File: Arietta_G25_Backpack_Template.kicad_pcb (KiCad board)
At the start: 2 copper layers, 26.7 x 53.3 mm, 1 part, among them P1 HEADER_F_2.54MM_2R40P_ST_AU_P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

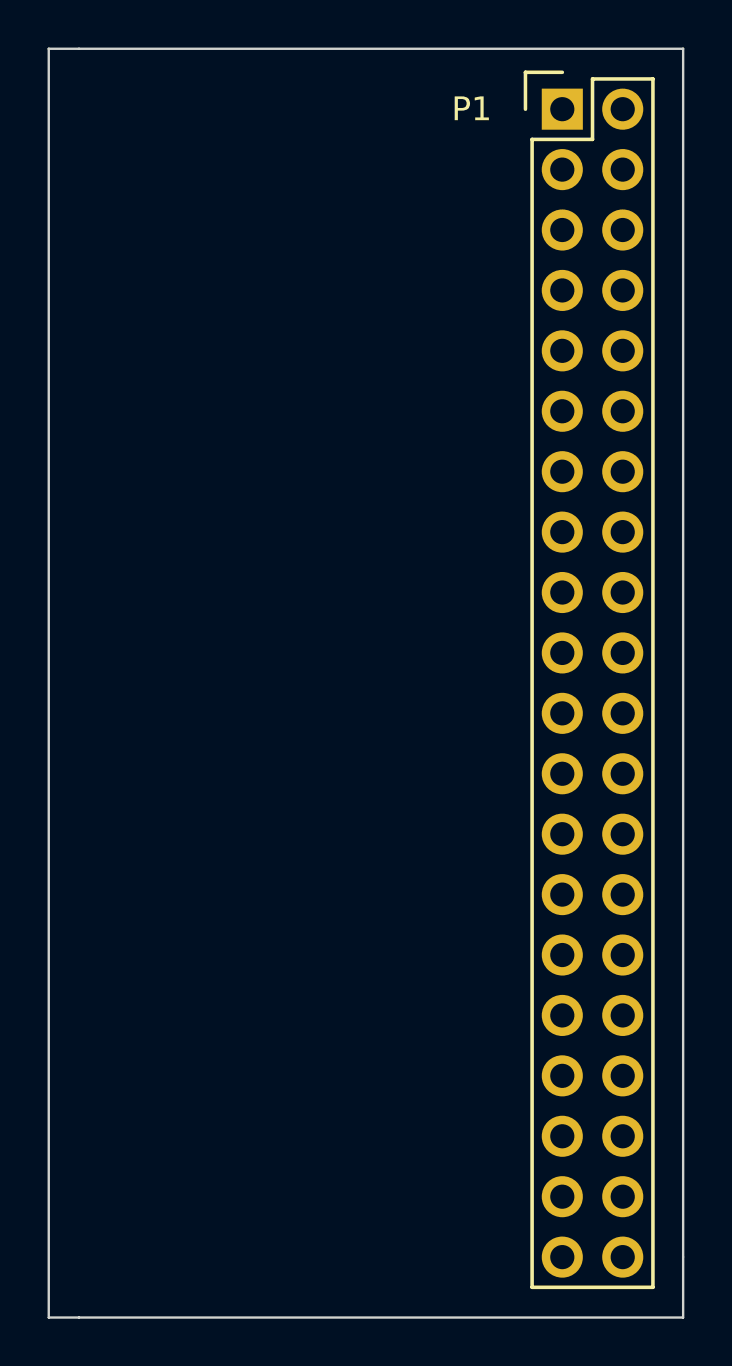
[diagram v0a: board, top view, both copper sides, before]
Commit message: Changed connector on PCB to use one in local library.
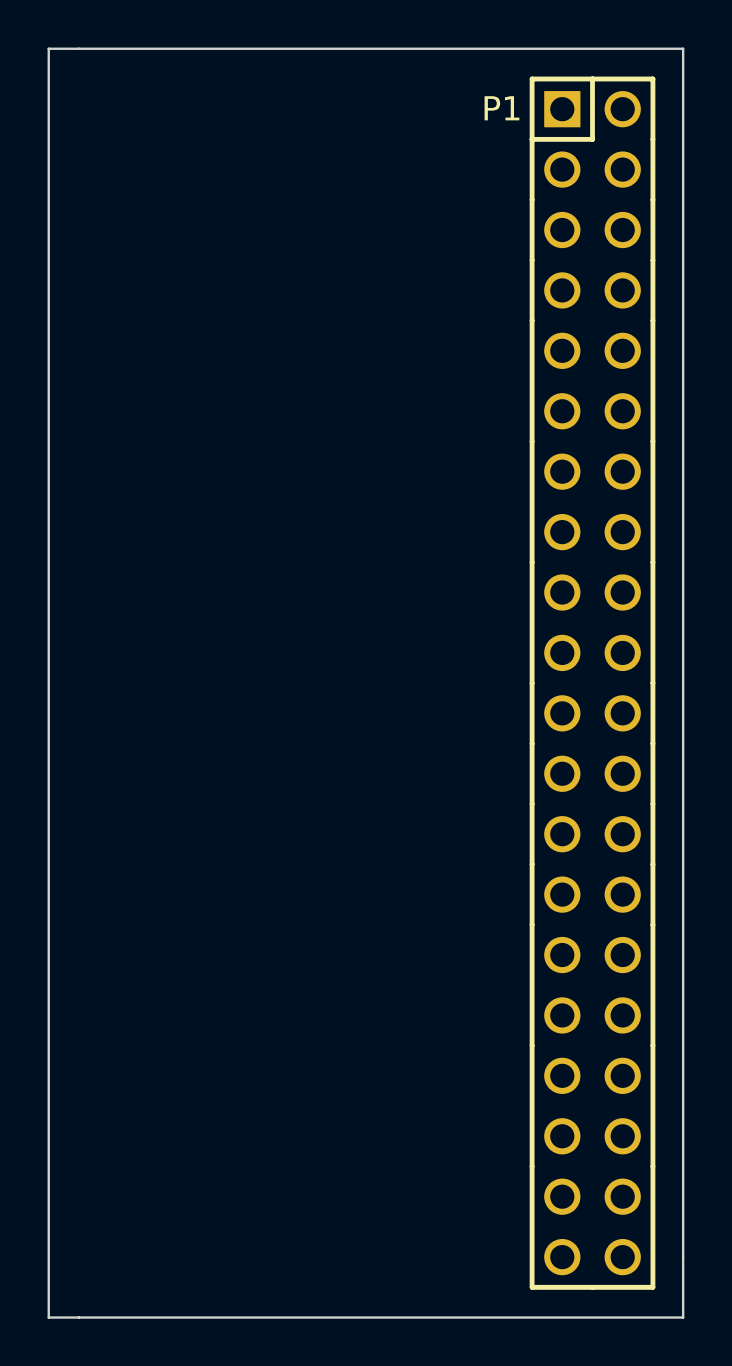
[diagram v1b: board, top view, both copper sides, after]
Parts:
- P1: value HEADER_F_2.54MM_2R40P_ST_AU_PTH -> (none); footprint Pin_Headers:Pin_Header_Straight_2x20 -> Header:HEADER_M_2.54MM_2R40P_ST_AU_PTH
- moved P1 24.2 mm to (184.2, 77.5), turned to 270 degrees
